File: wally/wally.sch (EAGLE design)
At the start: 12 parts, among them IC1 ESP32-S3-WROOM-1-N4, J6 USBC, U1 RA-01H

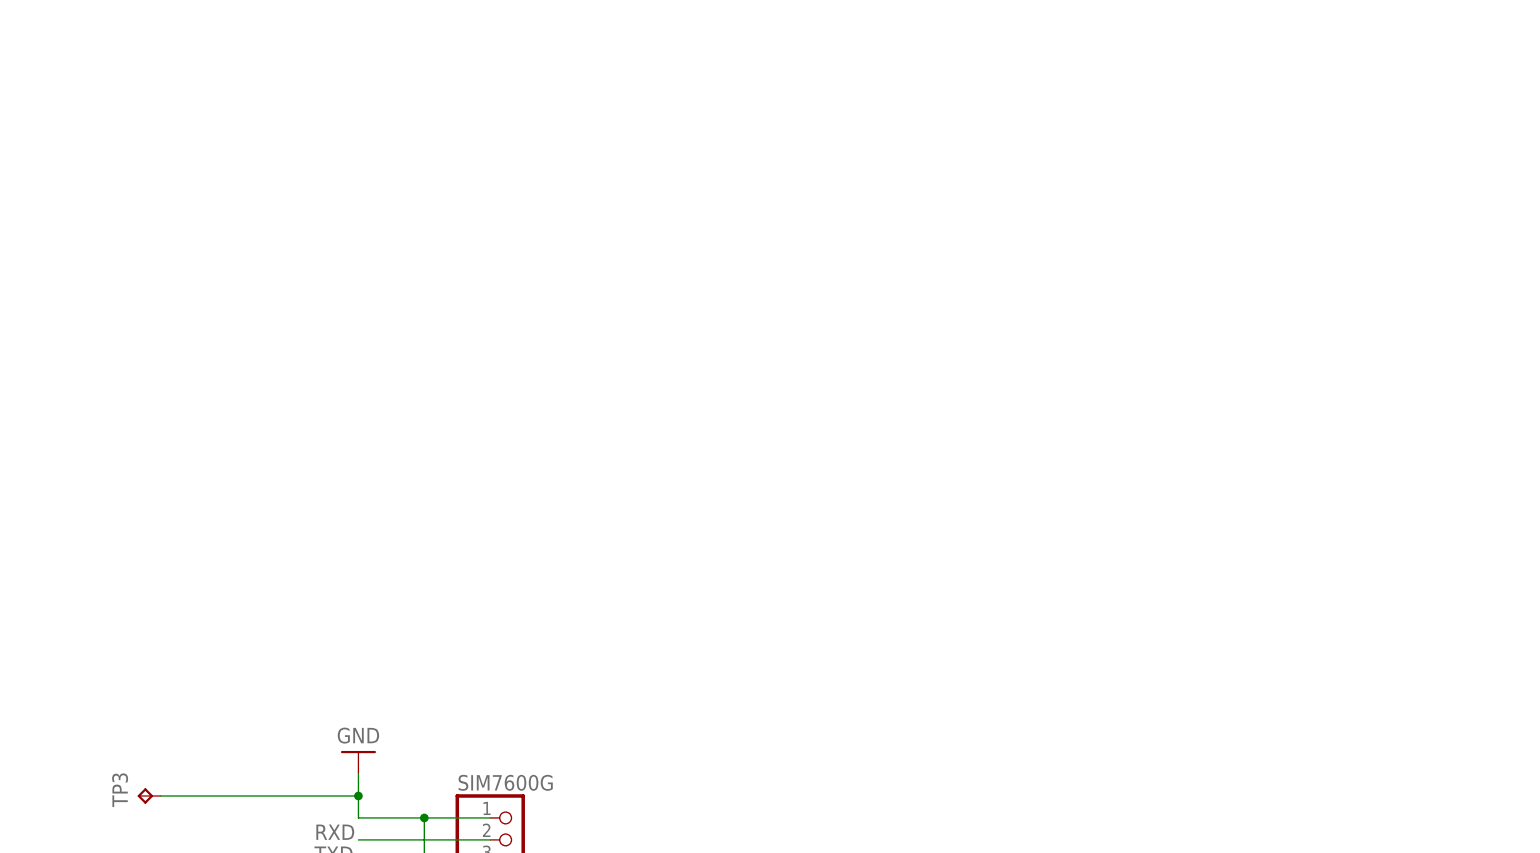
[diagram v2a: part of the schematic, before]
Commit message: Boost circuit for SIM
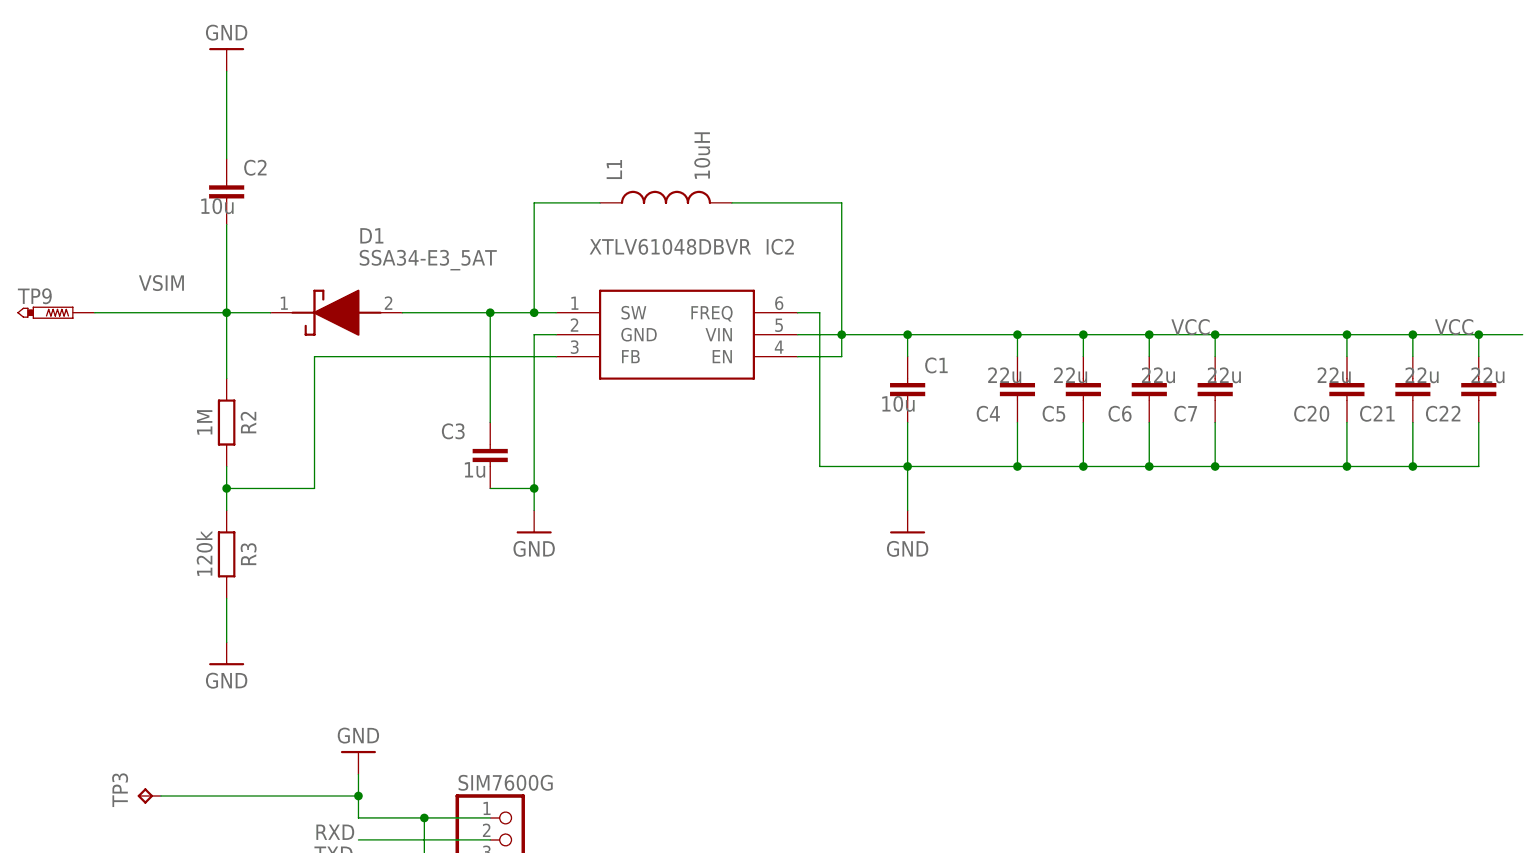
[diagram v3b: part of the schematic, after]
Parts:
- added C1, C2: 10u, Capacitor:C_CHIP-0603(1608-METRIC)
- added C20, C21, C22, C4, C5, C6, C7: 22u, Capacitor:C_CHIP-0603(1608-METRIC)
- added C3: 1u, Capacitor:C_CHIP-0603(1608-METRIC)
- added D1: SSA34-E3_5AT, SamacSys_Parts:SSA34-E3_5AT
- added IC2: XTLV61048DBVR, SamacSys_Parts:XTLV61048DBVR
- added L1: 10uH, BeagleBone_Blue_R3:INDUCTOR
- added R2: 1M, Resistor:R_CHIP-0603(1608-METRIC)
- added R3: 120k, Resistor:R_CHIP-0603(1608-METRIC)
- added TP9: PTR1PAD1-13, testpad:PTR1PAD1-13
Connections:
- new net N$2: C3.1, D1.A, IC2.SW, L1.1
- new net N$3: IC2.FB, R2.2, R3.1
- new net VCC: C1.1, C20.2, C21.2, C22.2, C4.2, C5.2, C6.2, C7.2, IC2.EN, IC2.VIN, L1.2
- net GND: now also C1.2, C2.1, C20.1, C21.1, C22.1, C3.2, C4.1, C5.1, C6.1, C7.1, IC2.FREQ, IC2.GND, R3.2
- net VSIM: now also C2.2, D1.K, R2.1, TP9.TP

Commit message: battery inputs
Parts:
- added CN1, CN2: (no value), adafruit:JST_2PIN-THM-RA
- added J3: S2B-PH-K-S(LF)(SN), Connectors:S2B-PH-K-S(LF)(SN)
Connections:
- net GND: now also CN1.1, CN2.1
- net VCC: now also CN1.2, CN2.2
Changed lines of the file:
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@@
 <part name="C21" library="Capacitor" library_urn="urn:adsk.eagle:library:16290819" deviceset="C" device="CHIP-0603(1608-METRIC)" package3d_urn="urn:adsk.eagle:package:16290898/5" technology="_" value="22u"/>
 <part name="C22" library="Capacitor" library_urn="urn:adsk.eagle:library:16290819" deviceset="C" device="CHIP-0603(1608-METRIC)" package3d_urn="urn:adsk.eagle:package:16290898/5" technology="_" value="22u"/>
+<part name="J3" library="Connectors" library_urn="urn:adsk.eagle:library:28493002" deviceset="S2B-PH-K-S(LF)(SN)" device="" package3d_urn="urn:adsk.eagle:package:10989924/2"/>
+<part name="CN1" library="adafruit" library_urn="urn:adsk.eagle:library:420" deviceset="JST_2PIN" device="-THM-RA" package3d_urn="urn:adsk.eagle:package:6240694/1"/>
+<part name="CN2" library="adafruit" library_urn="urn:adsk.eagle:library:420" deviceset="JST_2PIN" device="-THM-RA" package3d_urn="urn:adsk.eagle:package:6240694/1"/>
 </parts>
 <sheets>
@@
 <attribute name="NAME" x="97.155" y="210.185" size="1.778" layer="95" rot="R180"/>
 <attribute name="VALUE" x="102.235" y="214.63" size="1.778" layer="96" rot="R180"/>
+</instance>
+<instance part="J3" gate="G$1" x="0" y="-99.06" smashed="yes">
+<attribute name="NAME" x="-5.08" y="-95.758" size="1.778" layer="95"/>
+<attribute name="VALUE" x="-5.08" y="-106.68" size="1.778" layer="96"/>
+</instance>
+<instance part="CN1" gate="G$1" x="-25.4" y="281.94" smashed="yes">
+<attribute name="NAME" x="-31.75" y="287.655" size="1.778" layer="95"/>
+<attribute name="VALUE" x="-31.75" y="276.86" size="1.778" layer="96"/>
+</instance>
+<instance part="CN2" gate="G$1" x="-25.4" y="269.24" smashed="yes">
+<attribute name="NAME" x="-31.75" y="274.955" size="1.778" layer="95"/>
+<attribute name="VALUE" x="-31.75" y="264.16" size="1.778" layer="96"/>
 </instance>
 </instances>
@@
 <pinref part="C2" gate="G$1" pin="1"/>
 <pinref part="SUPPLY8" gate="G$1" pin="GND"/>
-<wire x1="-45.72" y1="238.76" x2="-45.72" y2="248.92" width="0.1524" layer="91"/>
+<wire x1="-45.72" y1="238.76" x2="-45.72" y2="243.84" width="0.1524" layer="91"/>
+<pinref part="CN1" gate="G$1" pin="1"/>
+<wire x1="-45.72" y1="243.84" x2="-45.72" y2="248.92" width="0.1524" layer="91"/>
+<wire x1="-27.94" y1="284.48" x2="-50.8" y2="284.48" width="0.1524" layer="91"/>
+<wire x1="-50.8" y1="284.48" x2="-50.8" y2="243.84" width="0.1524" layer="91"/>
+<wire x1="-50.8" y1="243.84" x2="-45.72" y2="243.84" width="0.1524" layer="91"/>
+<junction x="-45.72" y="243.84"/>
+<pinref part="CN2" gate="G$1" pin="1"/>
+<wire x1="-27.94" y1="271.78" x2="-40.64" y2="271.78" width="0.1524" layer="91"/>
+<wire x1="-40.64" y1="271.78" x2="-40.64" y2="243.84" width="0.1524" layer="91"/>
+<wire x1="-40.64" y1="243.84" x2="-45.72" y2="243.84" width="0.1524" layer="91"/>
 </segment>
 <segment>
@@
 <junction x="83.82" y="218.44"/>
 </segment>
-</net>
+<segment>
+<pinref part="CN2" gate="G$1" pin="2"/>
+<wire x1="-27.94" y1="269.24" x2="-38.1" y2="269.24" width="0.1524" layer="91"/>
+<wire x1="-38.1" y1="269.24" x2="-38.1" y2="281.94" width="0.1524" layer="91"/>
+<pinref part="CN1" gate="G$1" pin="2"/>
+<wire x1="-38.1" y1="281.94" x2="-27.94" y2="281.94" width="0.1524" layer="91"/>
+<label x="-35.56" y="264.16" size="1.778" layer="95"/>
+</segment>
+</net>

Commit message: LDO for 3v3
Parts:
- removed J3: S2B-PH-K-S(LF)(SN), Connectors:S2B-PH-K-S(LF)(SN)
- added C10, C8: 1u, Capacitor:C_CHIP-0603(1608-METRIC)
- added C9: 100n, Capacitor:C_CHIP-0603(1608-METRIC)
- added IC3: TLV1117LV33DCYR, SamacSys_Parts:TLV1117LV33DCYR
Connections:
- net 3V3: now also C10.1, IC3.OUTPUT_1, IC3.OUTPUT_2
- net GND: now also C10.2, C8.2, C9.2, IC3.GND
- net N$26: now also J6.VBUS
- net VCC: now also C8.1, C9.1, IC3.INPUT
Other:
- moved on the sheet: CN1, CN2, U1

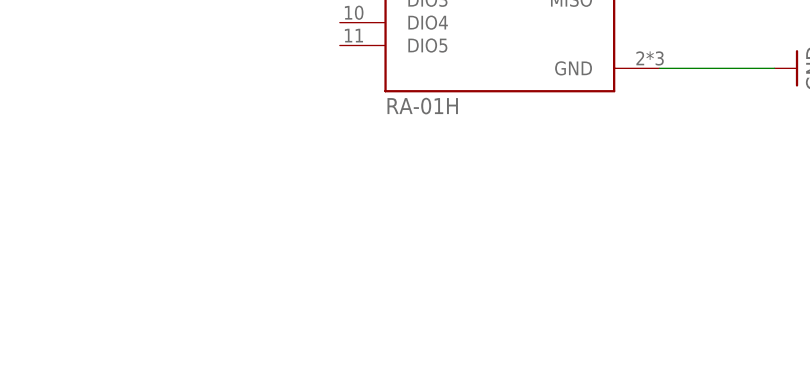
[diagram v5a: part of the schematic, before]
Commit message: add ds3231 rtc
treat as 5 pin header
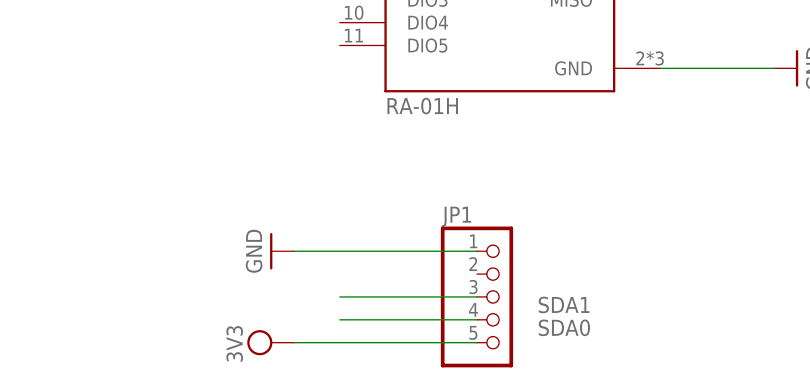
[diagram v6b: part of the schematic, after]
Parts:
- added JP1: (no value), pinhead:PINHD-1X5
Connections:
- new net SDA0: JP1.4
- new net SDA1: JP1.3
- net 3V3: now also JP1.5
- net GND: now also JP1.1
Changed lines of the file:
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@@
 <part name="C9" library="Capacitor" library_urn="urn:adsk.eagle:library:16290819" deviceset="C" device="CHIP-0603(1608-METRIC)" package3d_urn="urn:adsk.eagle:package:16290898/5" technology="_" value="100n"/>
 <part name="C10" library="Capacitor" library_urn="urn:adsk.eagle:library:16290819" deviceset="C" device="CHIP-0603(1608-METRIC)" package3d_urn="urn:adsk.eagle:package:16290898/5" technology="_" value="1u"/>
+<part name="JP1" library="pinhead" library_urn="urn:adsk.eagle:library:325" deviceset="PINHD-1X5" device="" package3d_urn="urn:adsk.eagle:package:22469/2"/>
+<part name="SUPPLY13" library="Power_Symbols" library_urn="urn:adsk.eagle:library:16502351" deviceset="GND-BAR" device="" value="GND"/>
+<part name="SUPPLY14" library="Power_Symbols" library_urn="urn:adsk.eagle:library:16502351" deviceset="3V3-CIRCLE" device="" value="3V3"/>
 </parts>
 <sheets>
@@
 <attribute name="NAME" x="8.255" y="37.465" size="1.778" layer="95" rot="R180"/>
 <attribute name="VALUE" x="5.715" y="44.45" size="1.778" layer="96" rot="R180"/>
+</instance>
+<instance part="JP1" gate="A" x="12.7" y="-152.4" smashed="yes">
+<attribute name="NAME" x="6.35" y="-144.145" size="1.778" layer="95"/>
+<attribute name="VALUE" x="6.35" y="-162.56" size="1.778" layer="96"/>
+</instance>
+<instance part="SUPPLY13" gate="G$1" x="-12.7" y="-147.32" smashed="yes" rot="R270">
+<attribute name="VALUE" x="-14.605" y="-147.32" size="1.778" layer="96" rot="R270" align="center"/>
+</instance>
+<instance part="SUPPLY14" gate="G$1" x="-12.7" y="-157.48" smashed="yes" rot="R90">
+<attribute name="VALUE" x="-15.875" y="-157.607" size="1.778" layer="96" rot="R90" align="bottom-center"/>
 </instance>
 </instances>
@@
 <wire x1="-7.62" y1="43.18" x2="2.54" y2="43.18" width="0.1524" layer="91"/>
 </segment>
+<segment>
+<pinref part="JP1" gate="A" pin="1"/>
+<wire x1="10.16" y1="-147.32" x2="-10.16" y2="-147.32" width="0.1524" layer="91"/>
+<pinref part="SUPPLY13" gate="G$1" pin="GND"/>
+</segment>
 </net>
 <net name="3V3" class="0">
@@
 <wire x1="2.54" y1="35.56" x2="17.78" y2="35.56" width="0.1524" layer="91"/>
 <wire x1="17.78" y1="35.56" x2="17.78" y2="30.48" width="0.1524" layer="91"/>
+</segment>
+<segment>
+<pinref part="JP1" gate="A" pin="5"/>
+<wire x1="10.16" y1="-157.48" x2="-10.16" y2="-157.48" width="0.1524" layer="91"/>
+<pinref part="SUPPLY14" gate="G$1" pin="3V3"/>
 </segment>
 </net>
@@
 </segment>
 </net>
+<net name="SDA0" class="0">
+<segment>
+<pinref part="JP1" gate="A" pin="4"/>
+<wire x1="10.16" y1="-154.94" x2="-5.08" y2="-154.94" width="0.1524" layer="91"/>
+<label x="22.86" y="-154.94" size="1.778" layer="95" rot="R180"/>
+</segment>
+</net>
+<net name="SDA1" class="0">
+<segment>
+<pinref part="JP1" gate="A" pin="3"/>
+<wire x1="10.16" y1="-152.4" x2="-5.08" y2="-152.4" width="0.1524" layer="91"/>
+<label x="22.86" y="-152.4" size="1.778" layer="95" rot="R180"/>
+</segment>
+</net>

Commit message: reset switch
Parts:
- added C11, C13, C16: 100n, Capacitor:C_CHIP-0603(1608-METRIC)
- added C12: 22u, Capacitor:C_CHIP-0603(1608-METRIC)
- added R1: 10k, Resistor:R_CHIP-0603(1608-METRIC)
- added R4: 1k, Resistor:R_CHIP-0603(1608-METRIC)
- added S1: TS-1187A-B-A-B, SamacSys_Parts:TS-1187A-B-A-B
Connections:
- removed net USB_D+: J6.D+
- removed net USB_D-: J6.D-
- new net EN: R4.2
- new net N$1: C13.1, IC1.EN, R1.2
- new net N$4: C16.2, R4.1, S1.COM_1, S1.COM_2
- new net USB_N: IC1.IO19, J6.D-
- new net USB_P: IC1.IO20, J6.D+
- net 3V3: now also C11.1, C12.1, R1.1
- net GND: now also C11.2, C12.2, C13.2, C16.1, S1.NO_1, S1.NO_2

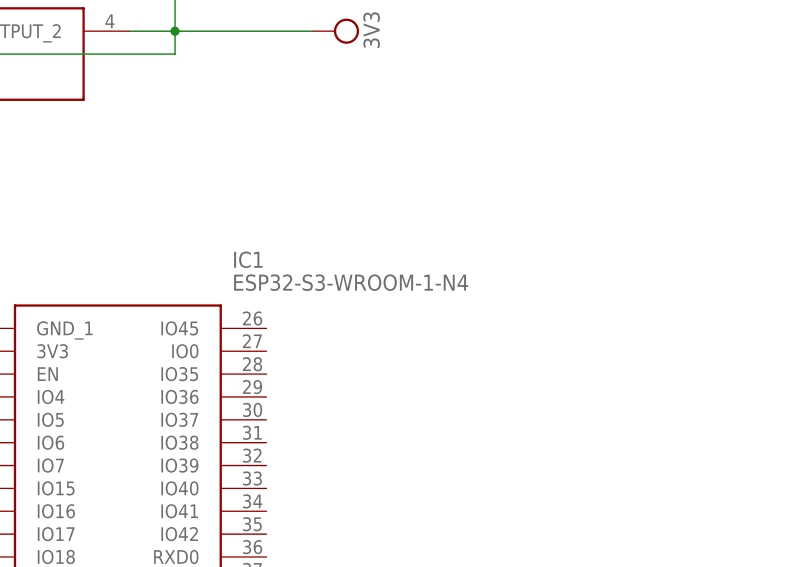
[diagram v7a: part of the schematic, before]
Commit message: switch to smaller esp
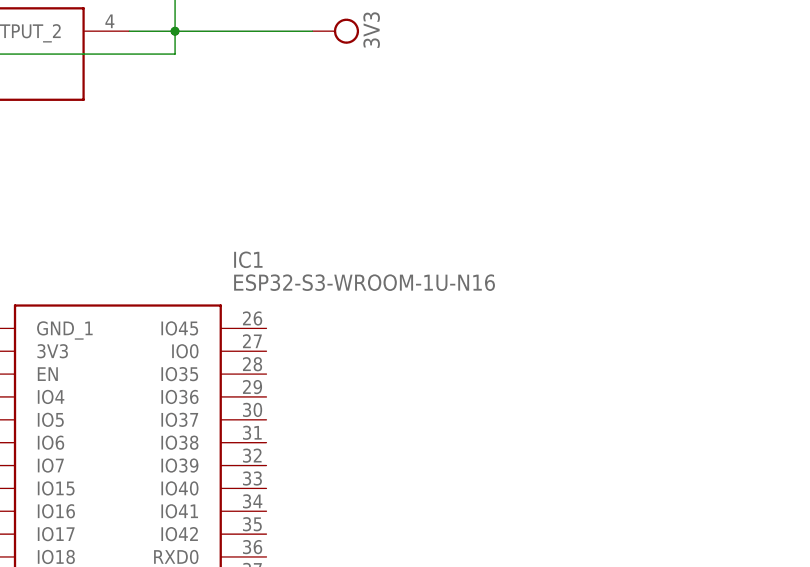
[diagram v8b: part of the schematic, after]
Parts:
- IC1: value ESP32-S3-WROOM-1-N4 -> ESP32-S3-WROOM-1U-N16; device SamacSys_Parts:ESP32-S3-WROOM-1-N4 -> SamacSys_Parts:ESP32-S3-WROOM-1U-N16
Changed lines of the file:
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@@
 <parts>
 <part name="U1" library="RA-01H" deviceset="RA-01H" device=""/>
-<part name="IC1" library="SamacSys_Parts" deviceset="ESP32-S3-WROOM-1-N4" device=""/>
+<part name="IC1" library="SamacSys_Parts" deviceset="ESP32-S3-WROOM-1U-N16" device=""/>
 <part name="SUPPLY1" library="Power_Symbols" library_urn="urn:adsk.eagle:library:16502351" deviceset="GND-BAR" device="" value="GND"/>
 <part name="SUPPLY2" library="Power_Symbols" library_urn="urn:adsk.eagle:library:16502351" deviceset="GND-BAR" device="" value="GND"/>
